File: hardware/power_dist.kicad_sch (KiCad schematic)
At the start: 15 parts, among them U1 TPS62175DQC, U7 LT1962-3.3

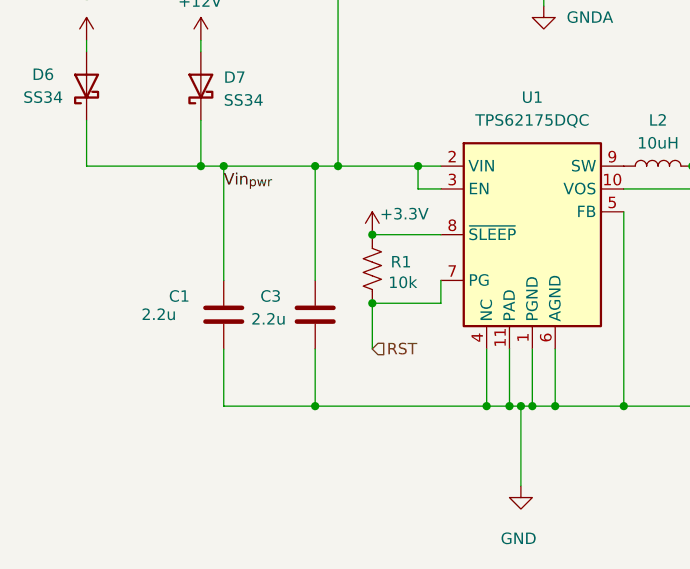
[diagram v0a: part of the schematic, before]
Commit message: Refactor netlist and lock footprints in PCB design
Renamed the /RESET net to /~{RESET} and updated all references accordingly. Reordered and renumbered net definitions to maintain consistency. Added the 'locked' attribute to multiple footprints for improved layout stability. Updated silkscreen reference positions for R8 and R10. No functional changes to the schematic or board layout.
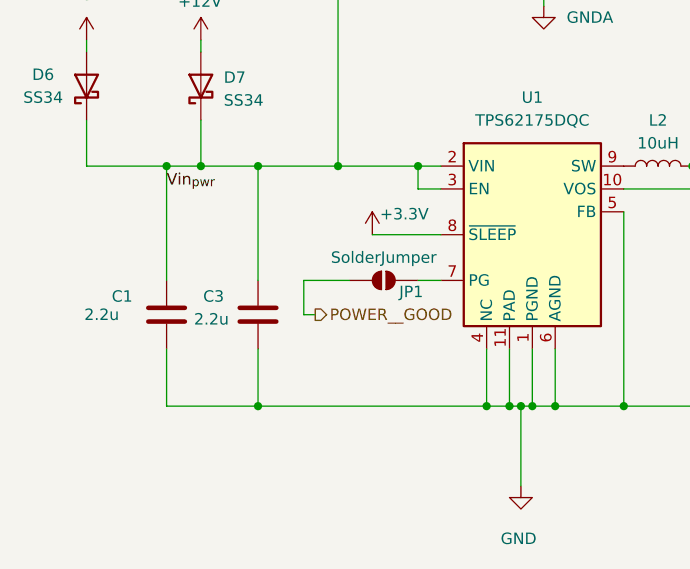
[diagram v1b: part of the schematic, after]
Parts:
- removed R1: 10k, Resistor_SMD:R_0603_1608Metric, symbol Device:R_US
- added JP1: SolderJumper, Jumper:SolderJumper-2_P1.3mm_Open_TrianglePad1.0x1.5mm, symbol Jumper:SolderJumper_2_Open
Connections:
- net RST: no longer names the net of U1.7 (PG)
- net RST: now also JP1.2 (B)
- new net POWER__GOOD: JP1.1 (A)
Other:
- moved on the sheet: C1, C3

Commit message: changed to in-stock buck regulator
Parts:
- removed U1: TPS62175DQC, Package_SON:WSON-10-1EP_2x3mm_P0.5mm_EP0.84x2.4mm_ThermalVias, symbol Regulator_Switching:TPS62175DQC
- added U8: TPS62177DQC, Package_SON:WSON-10-1EP_2x3mm_P0.5mm_EP0.84x2.4mm_ThermalVias, symbol Regulator_Switching:TPS62177DQC
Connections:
- net +3.3V: now also U8.10 (VOS), U8.8 (~{SLEEP})
- net GND: now also U8.1 (PGND), U8.11 (PAD), U8.4 (NC), U8.5 (FB), U8.6 (AGND)
- net Vin_{pwr}: now also U8.2 (VIN), U8.3 (EN)
- net at L2.1: now also U8.9 (SW)
- net at JP1.2 (B): now also U8.7 (PG)
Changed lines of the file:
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@@
+	)
+	(symbol
+		(lib_id "Regulator_Switching:TPS62177DQC")
+		(at 106.68 66.04 0)
+		(unit 1)
+		(exclude_from_sim no)
+		(in_bom yes)
+		(on_board yes)
+		(dnp no)
+		(fields_autoplaced yes)
+		(property "Reference" "U8"
+			(at 106.68 50.8 0)
+			(effects
+				(font
+					(size 1.27 1.27)
+				)
+			)
+		)
+		(property "Value" "TPS62177DQC"
+			(at 106.68 53.34 0)
+			(effects
+				(font
+					(size 1.27 1.27)
+				)
+			)
+		)
+		(property "Footprint" "Package_SON:WSON-10-1EP_2x3mm_P0.5mm_EP0.84x2.4mm_ThermalVias"
+			(at 110.49 77.47 0)
+			(effects
+				(font
+					(size 1.27 1.27)
+				)
+				(justify left)
+				(hide yes)
+			)
+		)
+		(property "Datasheet" "http://www.ti.com/lit/ds/symlink/tps62177.pdf"
+			(at 106.68 52.07 0)
+			(effects
+				(font
+					(size 1.27 1.27)
+				)
+				(hide yes)
+			)
+		)
+		(property "Description" "500mA Step-Down Converter with Sleep Mode, fixed 3.3V Output Voltage, 4.75-28V input voltage, WSON-10"
+			(at 106.68 66.04 0)
+			(effects
+				(font
+					(size 1.27 1.27)
+				)
+				(hide yes)
+			)
+		)
+		(property "LCSC" "C91241"
+			(at 106.68 66.04 0)
+			(effects
+				(font
+					(size 1.27 1.27)
+				)
+				(hide yes)
+			)
+		)
+		(pin "9"
+		)
+		(pin "8"
+		)
+		(pin "7"
+		)
+		(pin "4"
+		)
+		(pin "11"
+		)
+		(pin "2"
+		)
+		(pin "3"
+		)
+		(pin "1"
+		)
+		(pin "6"
+		)
+		(pin "5"
+		)
+		(pin "10"
+		)
+		(instances
+			(project ""
+				(path "/594f9b09-cd7b-4dfb-a8eb-b099e26ad96c/bc2feb38-b1d3-42da-a90c-1ee53748a038"
+					(reference "U8")
+					(unit 1)
+				)
+			)
+		)
 	)
 	(symbol
@@
 					(unit 1)
 				)
-			)
-		)
-	)
-	(symbol
-		(lib_id "Regulator_Switching:TPS62175DQC")
-		(at 106.68 66.04 0)
-		(unit 1)
-		(exclude_from_sim no)
-		(in_bom yes)
-		(on_board yes)
-		(dnp no)
-		(fields_autoplaced yes)
-		(property "Reference" "U1"
-			(at 106.68 50.8 0)
-			(effects
-				(font
-					(size 1.27 1.27)
-				)
-			)
-		)
-		(property "Value" "TPS62175DQC"
-			(at 106.68 53.34 0)
-			(effects
-				(font
-					(size 1.27 1.27)
-				)
-			)
-		)
-		(property "Footprint" "Package_SON:WSON-10-1EP_2x3mm_P0.5mm_EP0.84x2.4mm_ThermalVias"
-			(at 110.49 77.47 0)
-			(effects
-				(font
-					(size 1.27 1.27)
-				)
-				(justify left)
-				(hide yes)
-			)
-		)
-		(property "Datasheet" "http://www.ti.com/lit/ds/symlink/tps62177.pdf"
-			(at 106.68 52.07 0)
-			(effects
-				(font
-					(size 1.27 1.27)
-				)
-				(hide yes)
-			)
-		)
-		(property "Description" "500mA Step-Down Converter with Sleep Mode, adjustable Output Voltage, 4.75-28V input voltage, WSON-10"
-			(at 106.68 66.04 0)
-			(effects
-				(font
-					(size 1.27 1.27)
-				)
-				(hide yes)
-			)
-		)
-		(property "LCSC" "C32097"
-			(at 106.68 66.04 0)
-			(effects
-				(font
-					(size 1.27 1.27)
-				)
-				(hide yes)
-			)
-		)
-		(pin "7"
-		)
-		(pin "8"
-		)
-		(pin "9"
-		)
-		(pin "11"
-		)
-		(pin "2"
-		)
-		(pin "3"
-		)
-		(pin "4"
-		)
-		(pin "5"
-		)
-		(pin "6"
-		)
-		(pin "1"
-		)
-		(pin "10"
-		)
-		(instances
-			(project "flight_stick"
-				(path "/594f9b09-cd7b-4dfb-a8eb-b099e26ad96c/bc2feb38-b1d3-42da-a90c-1ee53748a038"
-					(reference "U1")
-					(unit 1)
-				)
